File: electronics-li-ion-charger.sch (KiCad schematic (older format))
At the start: 16 parts, among them J1 Conn_01x01_Male, J2 Conn_01x01_Male, J3 USB_B_Micro, J4 Conn_01x03_Male, U1 MCP73831-2-OT

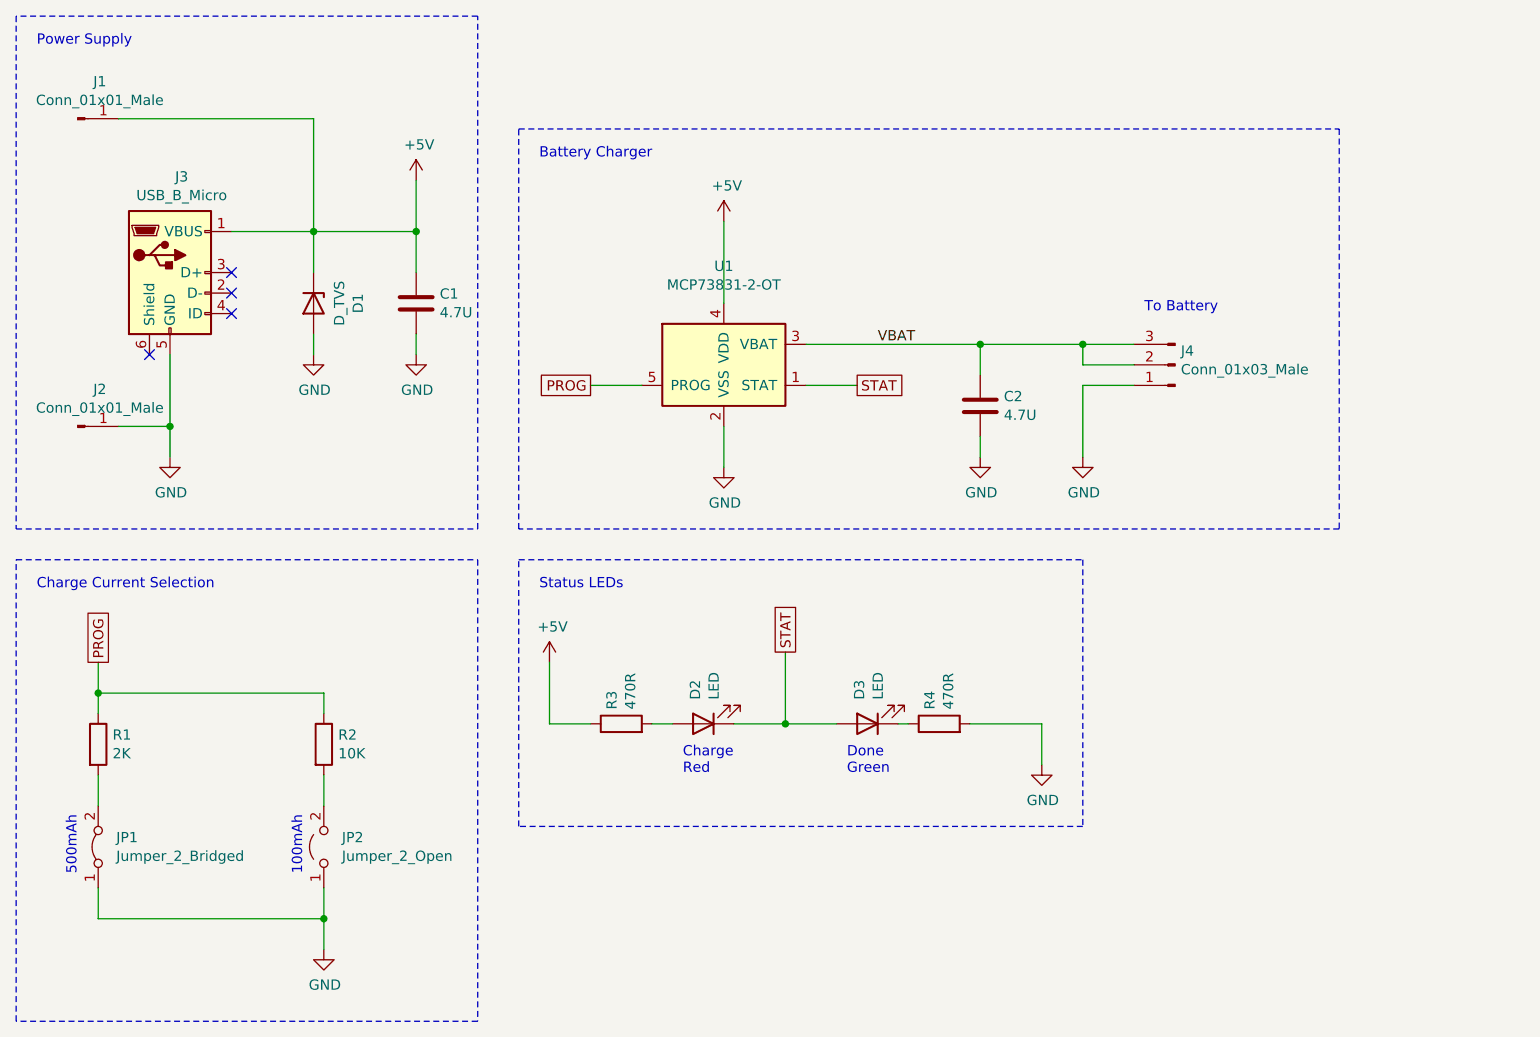
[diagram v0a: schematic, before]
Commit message: Add 18650 holder to schematic.
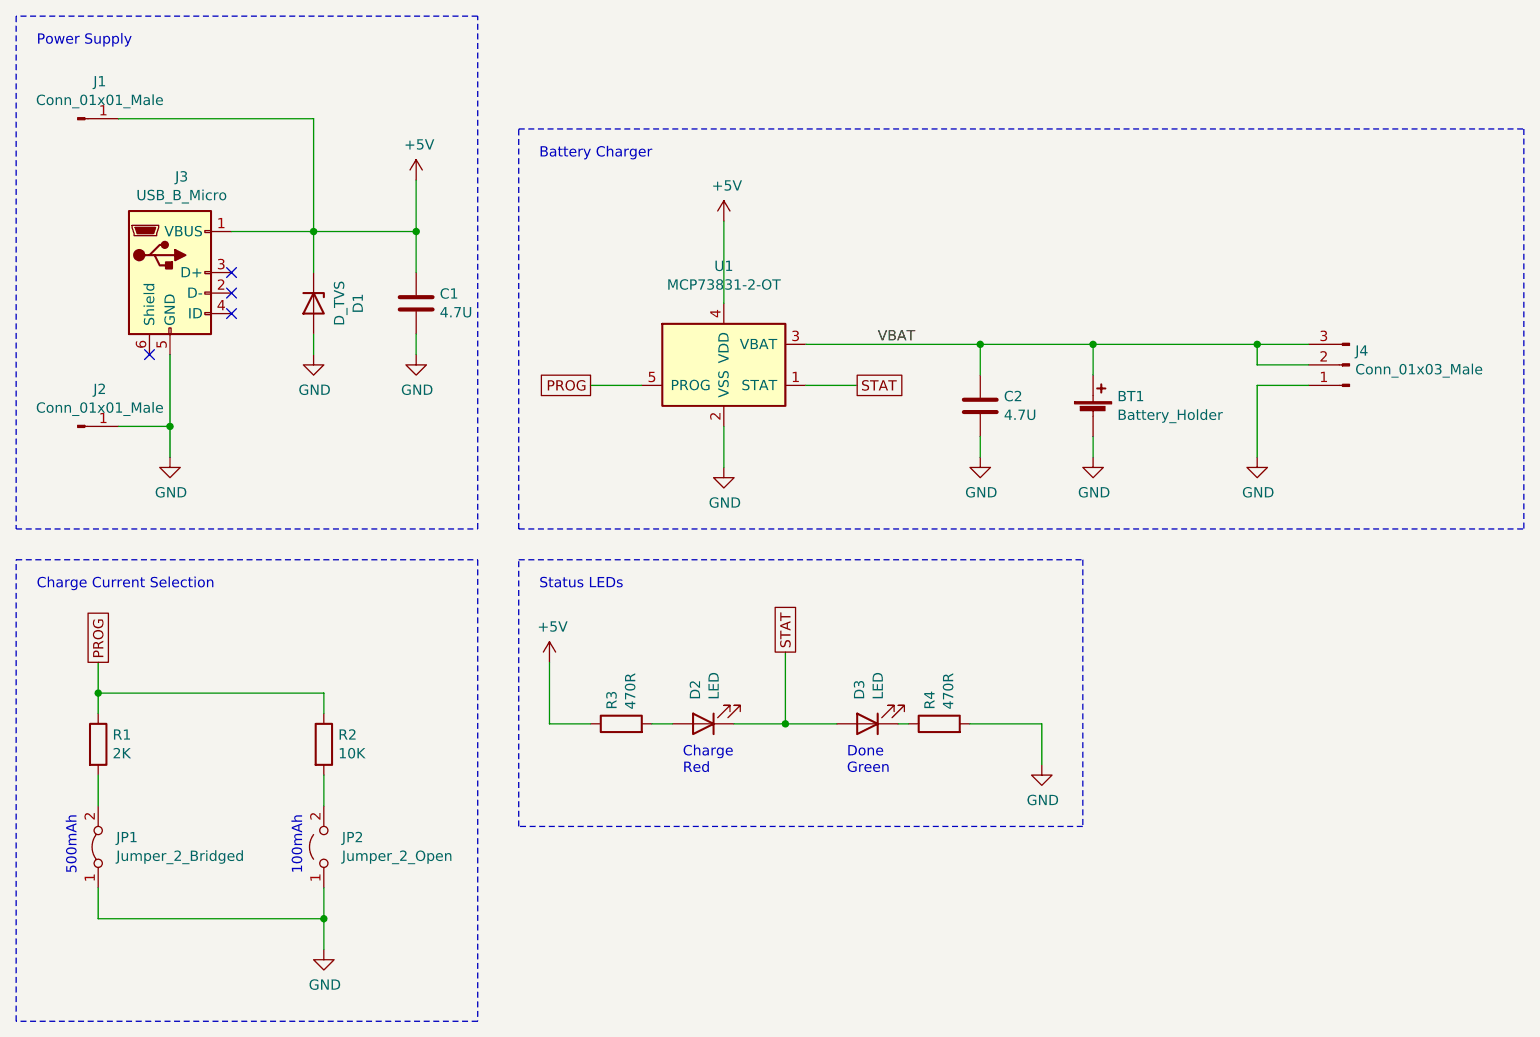
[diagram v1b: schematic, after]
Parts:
- added BT1: Battery_Holder, electronics-li-ion-charger:Battery_Holder-PC_Pin-18650, symbol Device:Battery_Cell
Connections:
- net GND: now also BT1.2 (-)
- net VBAT: now also BT1.1 (+)
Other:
- note removed: "To Battery"
- moved on the sheet: J4
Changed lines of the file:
@@
 L power:GND #PWR0101
 U 1 1 5FFBA88E
-P 7850 3650
-F 0 "#PWR0101" H 7850 3400 50  0001 C CNN
-F 1 "GND" H 7855 3477 50  0000 C CNN
-F 2 "" H 7850 3650 50  0001 C CNN
-F 3 "" H 7850 3650 50  0001 C CNN
-	1    7850 3650
+P 8700 3650
+F 0 "#PWR0101" H 8700 3400 50  0001 C CNN
+F 1 "GND" H 8705 3477 50  0000 C CNN
+F 2 "" H 8700 3650 50  0001 C CNN
+F 3 "" H 8700 3650 50  0001 C CNN
+	1    8700 3650
 	1    0    0    -1
 $EndComp
@@
 L Connector:Conn_01x03_Male J4
 U 1 1 5FFBF742
-P 8300 3200
-F 0 "J4" H 8272 3132 50  0000 R CNN
-F 1 "Conn_01x03_Male" H 8272 3223 50  0000 R CNN
-F 2 "Connector_PinHeader_2.54mm:PinHeader_1x03_P2.54mm_Vertical" H 8300 3200 50  0001 C CNN
-F 3 "~" H 8300 3200 50  0001 C CNN
-	1    8300 3200
+P 9150 3200
+F 0 "J4" H 9122 3132 50  0000 R CNN
+F 1 "Conn_01x03_Male" H 9122 3223 50  0000 R CNN
+F 2 "Connector_PinHeader_2.54mm:PinHeader_1x03_P2.54mm_Vertical" H 9150 3200 50  0001 C CNN
+F 3 "~" H 9150 3200 50  0001 C CNN
+	1    9150 3200
 	-1   0    0    1
 $EndComp
@@
 	7350 3100 7350 3250
 Wire Wire Line
-	7350 3100 7850 3100
-Wire Wire Line
-	8100 3200 7850 3200
-Wire Wire Line
-	7850 3200 7850 3100
-Connection ~ 7850 3100
-Wire Wire Line
-	7850 3100 8100 3100
-Wire Wire Line
-	8100 3300 7850 3300
-Wire Wire Line
-	7850 3300 7850 3650
+	8950 3200 8700 3200
+Wire Wire Line
+	8700 3200 8700 3100
+Connection ~ 8700 3100
+Wire Wire Line
+	8700 3100 8950 3100
+Wire Wire Line
+	8950 3300 8700 3300
+Wire Wire Line
+	8700 3300 8700 3650
 Wire Wire Line
 	7350 3550 7350 3650
@@
 Wire Wire Line
 	6500 3100 7350 3100
-Connection ~ 7350 3100
 $Comp
 L power:GND #PWR0105
@@
 Battery Charger
 Wire Notes Line
-	5100 2050 9100 2050
-Wire Notes Line
-	9100 2050 9100 4000
-Wire Notes Line
-	9100 4000 5100 4000
+	10000 2050 10000 4000
 Wire Notes Line
 	5100 4000 5100 2050
-Text Notes 8150 2950 0    50   ~ 0
-To Battery
 Wire Wire Line
 	4100 3050 4100 3150
@@
 	0    1    1    0
 $EndComp
+$Comp
+L Device:Battery_Cell BT1
+U 1 1 60035974
+P 7900 3450
+F 0 "BT1" H 8018 3546 50  0000 L CNN
+F 1 "Battery_Holder" H 8018 3455 50  0000 L CNN
+F 2 "electronics-li-ion-charger:Battery_Holder-PC_Pin-18650" V 7900 3510 50  0001 C CNN
+F 3 "~" V 7900 3510 50  0001 C CNN
+	1    7900 3450
+	1    0    0    -1
+$EndComp
+Wire Wire Line
+	7350 3100 7900 3100
+Connection ~ 7350 3100
+$Comp
+L power:GND #PWR03
+U 1 1 6003ECCA
+P 7900 3650
+F 0 "#PWR03" H 7900 3400 50  0001 C CNN
+F 1 "GND" H 7905 3477 50  0000 C CNN
+F 2 "" H 7900 3650 50  0001 C CNN
+F 3 "" H 7900 3650 50  0001 C CNN
+	1    7900 3650
+	1    0    0    -1
+$EndComp
+Wire Wire Line
+	7900 3550 7900 3650
+Wire Wire Line
+	7900 3100 7900 3250
+Wire Wire Line
+	7900 3100 8700 3100
+Connection ~ 7900 3100
+Wire Notes Line
+	5100 2050 10000 2050
+Wire Notes Line
+	5100 4000 10000 4000
 $EndSCHEMATC

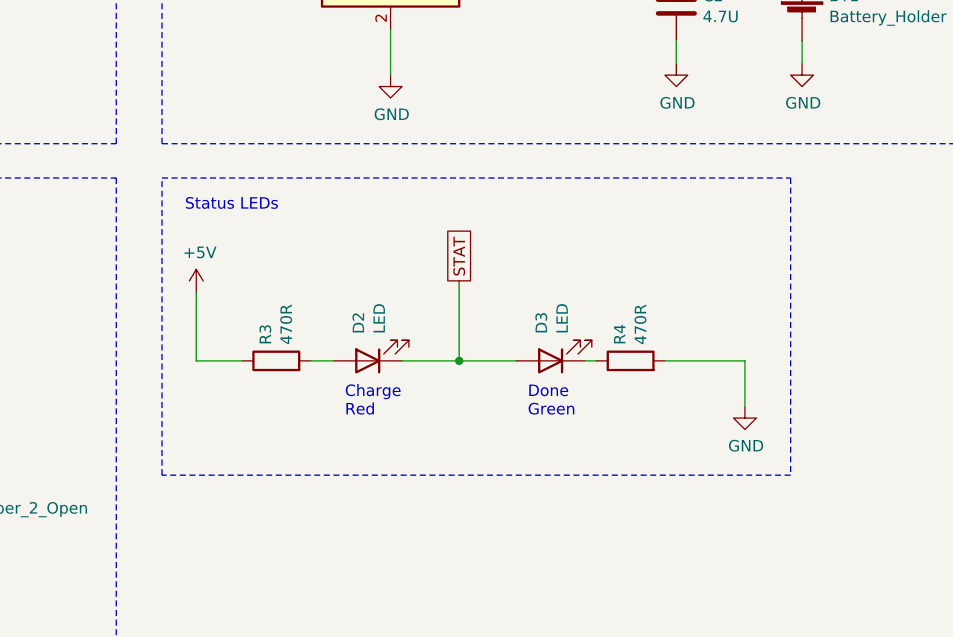
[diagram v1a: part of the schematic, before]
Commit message: Layout PCB with 18650 battery holder.
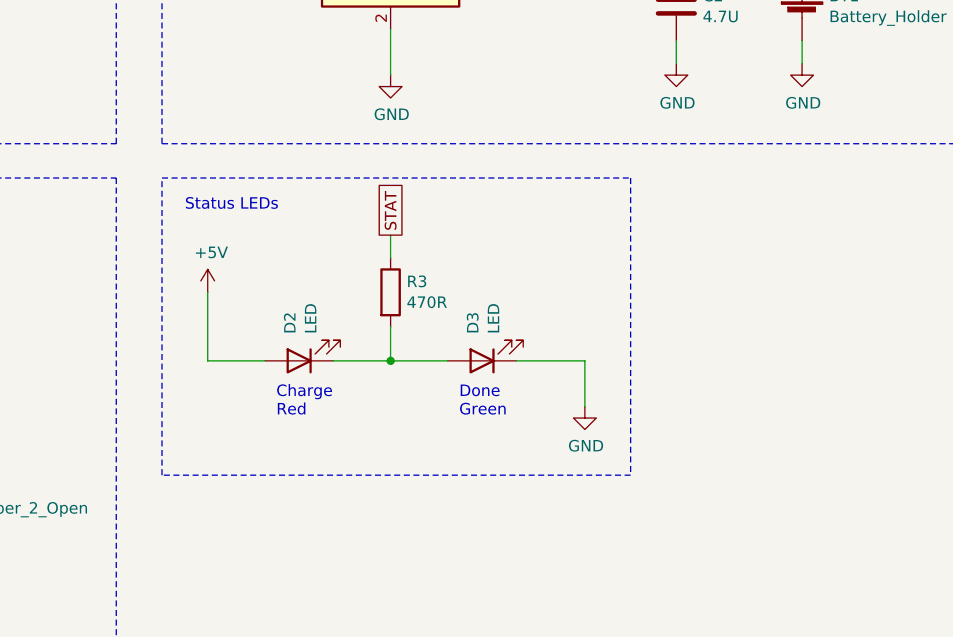
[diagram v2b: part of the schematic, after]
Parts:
- removed R4: 470R, Resistor_SMD:R_1206_3216Metric_Pad1.30x1.75mm_HandSolder, symbol Device:R
- JP1, JP2: footprint Connector_PinHeader_2.54mm:PinHeader_1x02_P2.54mm_Vertical -> Jumper:SolderJumper-2_P1.3mm_Open_TrianglePad1.0x1.5mm
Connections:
- net +5V: now also D2.2 (A); no longer R3.1
- net GND: now also D3.1 (K)
- net STAT: now also R3.1; no longer D2.1 (K), D3.2 (A)
- net at R3.2: now also D2.1 (K), D3.2 (A); no longer D2.2 (A)
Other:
- moved on the sheet: D2, D3, R3
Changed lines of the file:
@@
 $EndDescr
-$Comp
-L Device:R R4
-U 1 1 5FFB4EF8
-P 7150 4950
-F 0 "R4" H 7220 4996 50  0000 L CNN
-F 1 "470R" H 7220 4905 50  0000 L CNN
-F 2 "Resistor_SMD:R_1206_3216Metric_Pad1.30x1.75mm_HandSolder" V 7080 4950 50  0001 C CNN
-F 3 "~" H 7150 4950 50  0001 C CNN
-	1    7150 4950
-	0    -1   -1   0
-$EndComp
 $Comp
 L Device:R R3
 U 1 1 5FFB5567
-P 5600 4950
-F 0 "R3" H 5670 4996 50  0000 L CNN
-F 1 "470R" H 5670 4905 50  0000 L CNN
-F 2 "Resistor_SMD:R_1206_3216Metric_Pad1.30x1.75mm_HandSolder" V 5530 4950 50  0001 C CNN
-F 3 "~" H 5600 4950 50  0001 C CNN
-	1    5600 4950
-	0    -1   -1   0
+P 6100 4650
+F 0 "R3" H 6170 4696 50  0000 L CNN
+F 1 "470R" H 6170 4605 50  0000 L CNN
+F 2 "Resistor_SMD:R_1206_3216Metric_Pad1.30x1.75mm_HandSolder" V 6030 4650 50  0001 C CNN
+F 3 "~" H 6100 4650 50  0001 C CNN
+	1    6100 4650
+	1    0    0    -1
 $EndComp
 $Comp
@@
 L Device:LED D3
 U 1 1 5FFB6F7B
-P 6800 4950
-F 0 "D3" V 6839 4832 50  0000 R CNN
-F 1 "LED" V 6748 4832 50  0000 R CNN
-F 2 "LED_SMD:LED_1206_3216Metric_Pad1.42x1.75mm_HandSolder" H 6800 4950 50  0001 C CNN
-F 3 "~" H 6800 4950 50  0001 C CNN
-	1    6800 4950
+P 6500 4950
+F 0 "D3" V 6539 4832 50  0000 R CNN
+F 1 "LED" V 6448 4832 50  0000 R CNN
+F 2 "LED_SMD:LED_1206_3216Metric_Pad1.42x1.75mm_HandSolder" H 6500 4950 50  0001 C CNN
+F 3 "~" H 6500 4950 50  0001 C CNN
+	1    6500 4950
 	-1   0    0    1
 $EndComp
@@
 L Device:LED D2
 U 1 1 5FFB7C3E
-P 6000 4950
-F 0 "D2" V 6039 4832 50  0000 R CNN
-F 1 "LED" V 5948 4832 50  0000 R CNN
-F 2 "LED_SMD:LED_1206_3216Metric_Pad1.42x1.75mm_HandSolder" H 6000 4950 50  0001 C CNN
-F 3 "~" H 6000 4950 50  0001 C CNN
-	1    6000 4950
+P 5700 4950
+F 0 "D2" V 5739 4832 50  0000 R CNN
+F 1 "LED" V 5648 4832 50  0000 R CNN
+F 2 "LED_SMD:LED_1206_3216Metric_Pad1.42x1.75mm_HandSolder" H 5700 4950 50  0001 C CNN
+F 3 "~" H 5700 4950 50  0001 C CNN
+	1    5700 4950
 	-1   0    0    1
 $EndComp
@@
 	1    0    0    -1
 $EndComp
-Wire Wire Line
-	5750 4950 5850 4950
 $Comp
 L power:GND #PWR0106
@@
 F 0 "JP1" V 3096 5462 50  0000 R CNN
 F 1 "Jumper_2_Bridged" V 3005 5462 50  0000 R CNN
-F 2 "Connector_PinHeader_2.54mm:PinHeader_1x02_P2.54mm_Vertical" H 3050 5550 50  0001 C CNN
+F 2 "Jumper:SolderJumper-2_P1.3mm_Open_TrianglePad1.0x1.5mm" H 3050 5550 50  0001 C CNN
 F 3 "~" H 3050 5550 50  0001 C CNN
 	1    3050 5550
@@
 	1    0    0    -1
 $EndComp
-Wire Wire Line
-	6950 4950 7000 4950
 $Comp
 L power:GND #PWR02
@@
 F 0 "JP2" V 4196 5462 50  0000 R CNN
 F 1 "Jumper_2_Open" V 4105 5462 50  0000 R CNN
-F 2 "Connector_PinHeader_2.54mm:PinHeader_1x02_P2.54mm_Vertical" H 4150 5550 50  0001 C CNN
+F 2 "Jumper:SolderJumper-2_P1.3mm_Open_TrianglePad1.0x1.5mm" H 4150 5550 50  0001 C CNN
 F 3 "~" H 4150 5550 50  0001 C CNN
 	1    4150 5550
@@
 L power:+5V #PWR01
 U 1 1 60047041
-P 5250 4650
-F 0 "#PWR01" H 5250 4500 50  0001 C CNN
-F 1 "+5V" H 5265 4823 50  0000 C CNN
-F 2 "" H 5250 4650 50  0001 C CNN
-F 3 "" H 5250 4650 50  0001 C CNN
-	1    5250 4650
+P 5300 4650
+F 0 "#PWR01" H 5300 4500 50  0001 C CNN
+F 1 "+5V" H 5315 4823 50  0000 C CNN
+F 2 "" H 5300 4650 50  0001 C CNN
+F 3 "" H 5300 4650 50  0001 C CNN
+	1    5300 4650
 	1    0    0    -1
 $EndComp
 Text GLabel 6750 3300 2    50   UnSpc ~ 0
 STAT
-Text GLabel 6400 4600 1    50   UnSpc ~ 0
+Text GLabel 6100 4400 1    50   UnSpc ~ 0
 STAT
 Wire Wire Line
 	6500 3300 6750 3300
 Wire Wire Line
-	6400 4600 6400 4950
-Wire Wire Line
-	6150 4950 6400 4950
-Connection ~ 6400 4950
-Wire Wire Line
-	6400 4950 6650 4950
-Wire Wire Line
-	5250 4650 5250 4950
-Wire Wire Line
-	5250 4950 5450 4950
+	6100 4400 6100 4500
+Wire Wire Line
+	5850 4950 6100 4950
+Connection ~ 6100 4950
 Text Notes 2950 5400 3    50   ~ 0
 500mAh
@@
 Text Notes 5200 4300 0    50   ~ 0
 Status LEDs
-Text Notes 5900 5200 0    50   ~ 0
+Text Notes 5600 5200 0    50   ~ 0
 Charge\nRed
-Text Notes 6700 5200 0    50   ~ 0
+Text Notes 6400 5200 0    50   ~ 0
 Done\nGreen
 Wire Notes Line
-	5100 4150 7850 4150
-Wire Notes Line
-	7850 4150 7850 5450
-Wire Notes Line
-	7850 5450 5100 5450
-Wire Notes Line
 	5100 5450 5100 4150
 Wire Wire Line
 	6500 3100 7350 3100
-$Comp
-L power:GND #PWR0105
-U 1 1 5FFD2CF5
-P 7650 5150
-F 0 "#PWR0105" H 7650 4900 50  0001 C CNN
-F 1 "GND" H 7655 4977 50  0000 C CNN
-F 2 "" H 7650 5150 50  0001 C CNN
-F 3 "" H 7650 5150 50  0001 C CNN
-	1    7650 5150
-	1    0    0    -1
-$EndComp
-Wire Wire Line
-	7300 4950 7650 4950
-Wire Wire Line
-	7650 4950 7650 5150
 Text Notes 5200 2200 0    50   ~ 0
 Battery Charger
@@
 Wire Notes Line
 	5100 4000 10000 4000
+Wire Wire Line
+	6100 4800 6100 4950
+Wire Wire Line
+	6100 4950 6350 4950
+$Comp
+L power:GND #PWR0105
+U 1 1 5FFD2CF5
+P 6950 5150
+F 0 "#PWR0105" H 6950 4900 50  0001 C CNN
+F 1 "GND" H 6955 4977 50  0000 C CNN
+F 2 "" H 6950 5150 50  0001 C CNN
+F 3 "" H 6950 5150 50  0001 C CNN
+	1    6950 5150
+	1    0    0    -1
+$EndComp
+Wire Wire Line
+	5300 4650 5300 4950
+Wire Wire Line
+	5300 4950 5550 4950
+Wire Wire Line
+	6650 4950 6950 4950
+Wire Wire Line
+	6950 4950 6950 5150
+Wire Notes Line
+	5100 4150 7150 4150
+Wire Notes Line
+	7150 4150 7150 5450
+Wire Notes Line
+	7150 5450 5100 5450
 $EndSCHEMATC
